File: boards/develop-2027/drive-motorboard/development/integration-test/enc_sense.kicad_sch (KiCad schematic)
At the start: 5 parts, among them J4 PROG SPI, U6 AS5047P

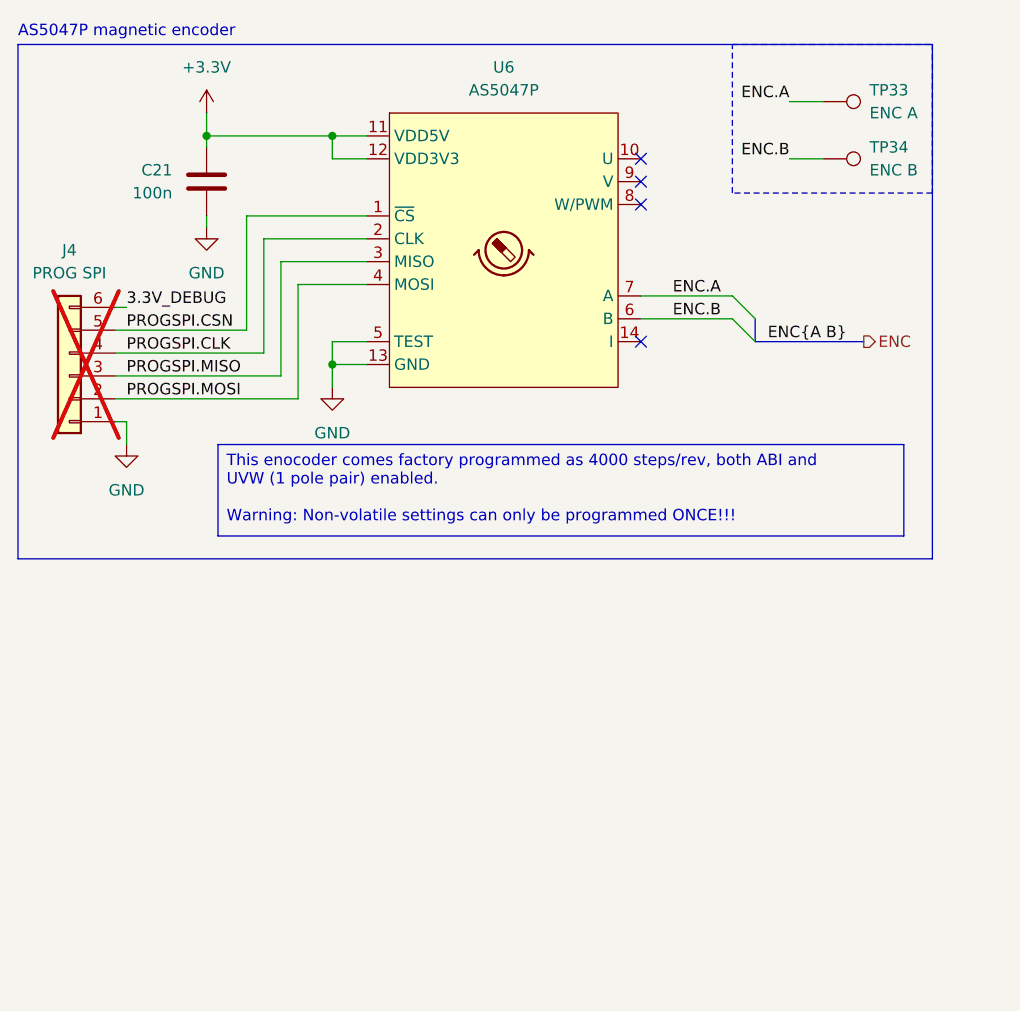
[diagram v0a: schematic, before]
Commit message: Set up PCB design rules
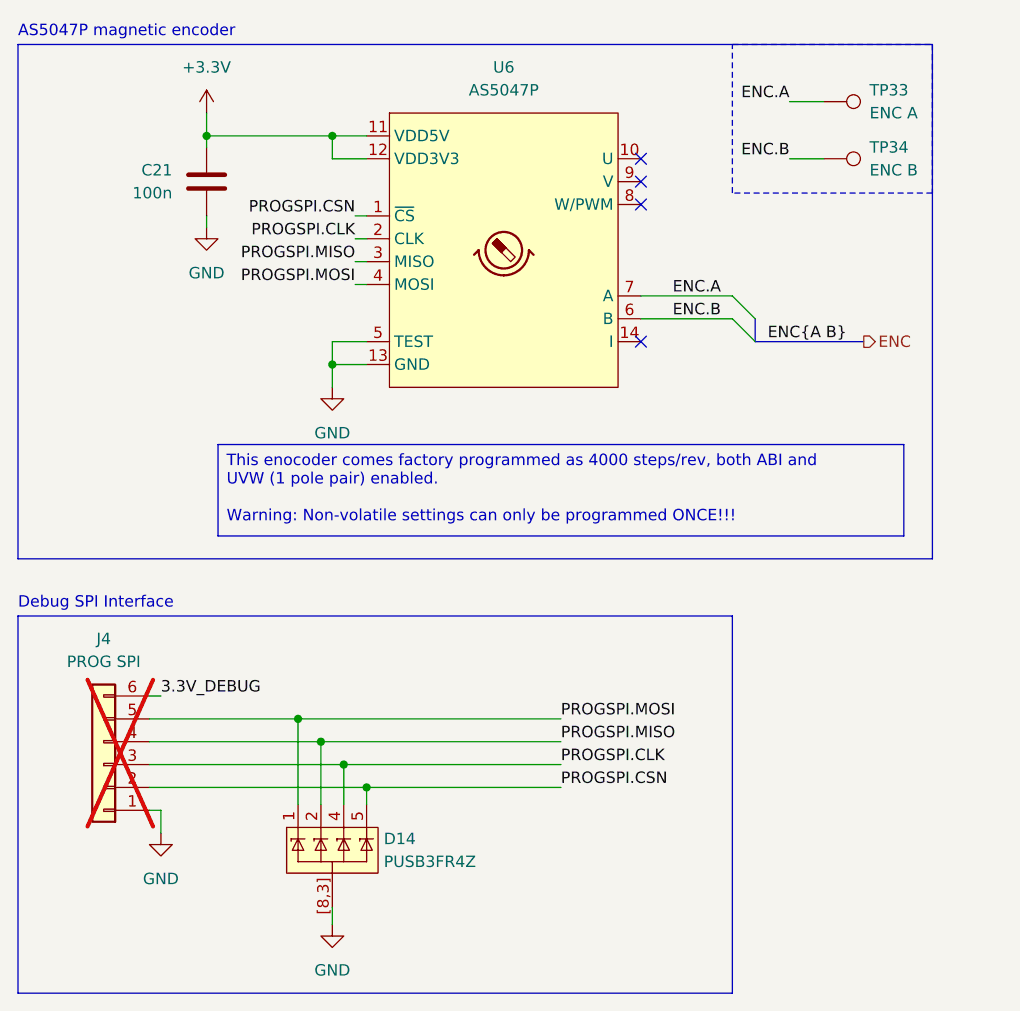
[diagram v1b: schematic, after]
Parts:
- added D14: PUSB3FR4Z, Package_DFN_QFN:Diodes_UDFN-10_1x2.5mm_P0.5mm, symbol RJ-Diodes:PUSB3FR4
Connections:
- net GND: now also D14.[8,3] (GND)
- net PROGSPI.CLK: now also J4.3 (Pin_3), D14.4 (CH3), D14.7 (CH3); no longer J4.4 (Pin_4)
- net PROGSPI.CSN: now also J4.2 (Pin_2), D14.5 (CH5), D14.6 (CH5); no longer J4.5 (Pin_5)
- net PROGSPI.MISO: now also J4.4 (Pin_4), D14.2 (CH2), D14.9 (CH2); no longer J4.3 (Pin_3)
- net PROGSPI.MOSI: now also J4.5 (Pin_5), D14.1 (CH1), D14.10 (CH1); no longer J4.2 (Pin_2)
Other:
- note added: "Debug SPI Interface"
